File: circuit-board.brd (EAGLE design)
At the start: 40.6 x 64.1 mm, 39 parts, among them Q1 BC547B, U1 MAX3232, U2 ATMEGA328P_TQFP, U3 ADUM1201BRZ, Y1 16MHz

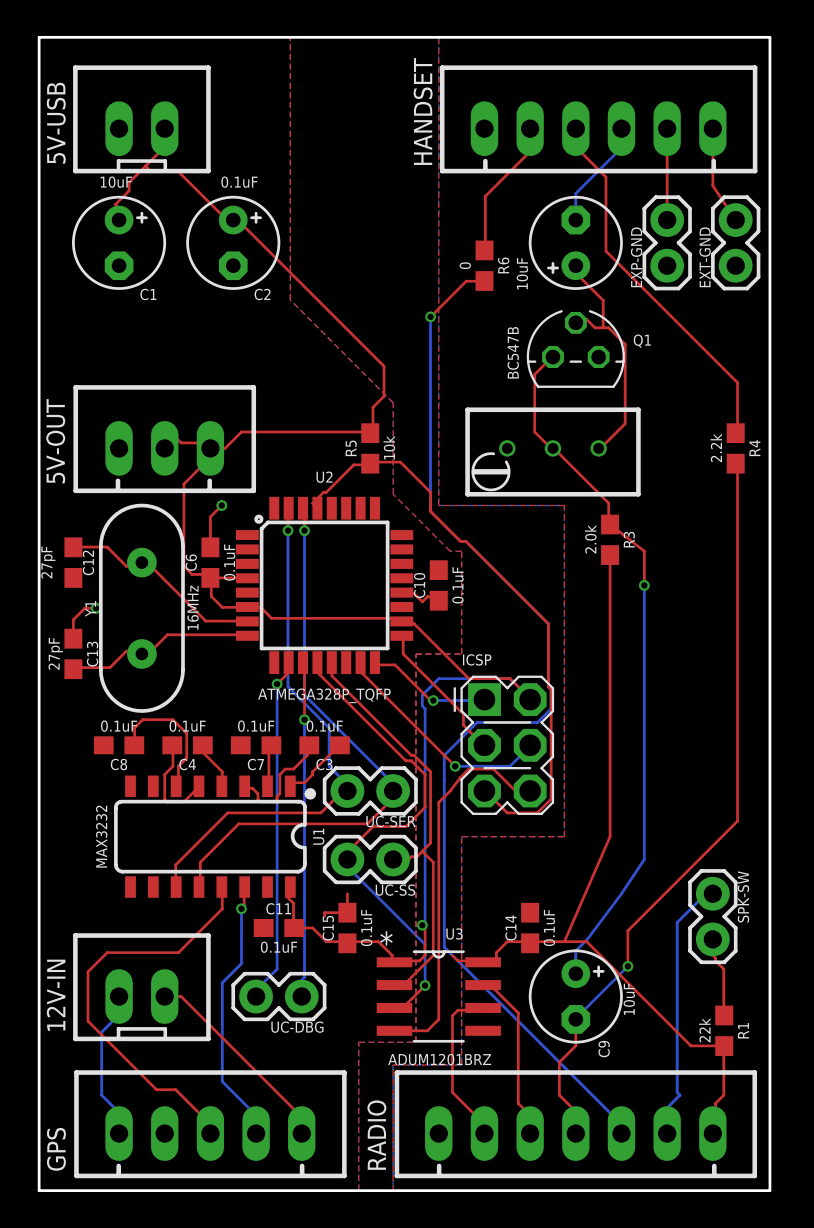
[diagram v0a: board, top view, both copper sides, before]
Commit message: Added labels for JST header pins, synced up board+schematic resistor values
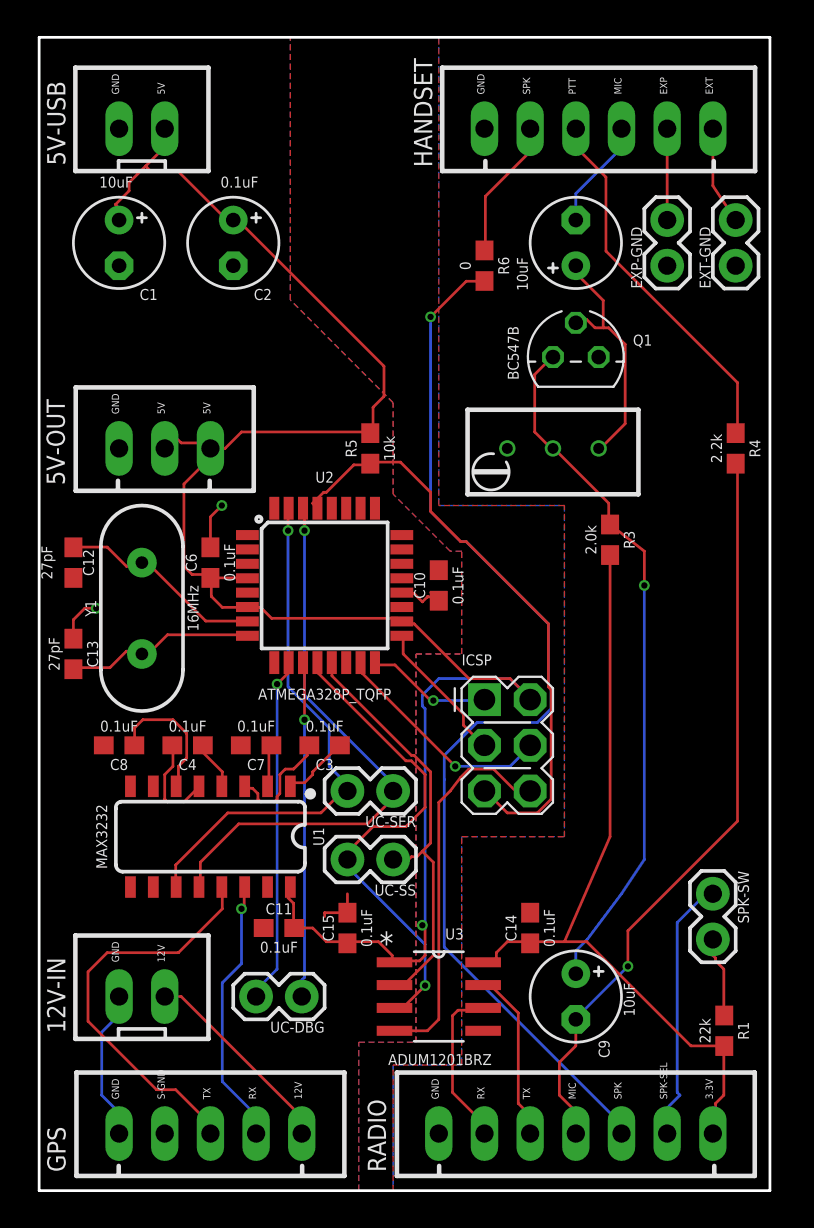
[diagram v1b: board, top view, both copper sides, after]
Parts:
- R2: value (none) -> 10k
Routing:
- net 3.3V: track 45.6 -> 43.8 mm
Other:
- board text added: "12V"
- board text added: "3.3V"
- board text added: "5V"
- board text added: "EXP"
- board text added: "EXT"
- board text added: "GND"
- board text added: "MIC"
- board text added: "PTT"
- board text added: "RX"
- board text added: "S-GND"
- board text added: "SPK"
- board text added: "SPK-SEL"
- board text added: "TX"
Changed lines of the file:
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@@
 github.com/paulmandal/radio-adapter
 v1.0</text>
+<text x="5.08" y="20.955" size="0.4064" layer="21" rot="R90">GND</text>
+<text x="7.62" y="20.955" size="0.4064" layer="21" rot="R90">S-GND</text>
+<text x="10.16" y="20.955" size="0.4064" layer="21" rot="R90">TX</text>
+<text x="12.7" y="20.955" size="0.4064" layer="21" rot="R90">RX</text>
+<text x="15.24" y="20.955" size="0.4064" layer="21" rot="R90">12V</text>
+<text x="22.86" y="20.955" size="0.4064" layer="21" rot="R90">GND</text>
+<text x="25.4" y="20.955" size="0.4064" layer="21" rot="R90">RX</text>
+<text x="27.94" y="20.955" size="0.4064" layer="21" rot="R90">TX</text>
+<text x="30.48" y="20.955" size="0.4064" layer="21" rot="R90">MIC</text>
+<text x="33.02" y="20.955" size="0.4064" layer="21" rot="R90">SPK</text>
+<text x="35.56" y="20.955" size="0.4064" layer="21" rot="R90">SPK-SEL</text>
+<text x="38.1" y="20.955" size="0.4064" layer="21" rot="R90">3.3V</text>
+<text x="5.08" y="28.575" size="0.4064" layer="21" rot="R90">GND</text>
+<text x="7.62" y="28.575" size="0.4064" layer="21" rot="R90">12V</text>
+<text x="5.08" y="59.055" size="0.4064" layer="21" rot="R90">GND</text>
+<text x="7.62" y="59.055" size="0.4064" layer="21" rot="R90">5V</text>
+<text x="10.16" y="59.055" size="0.4064" layer="21" rot="R90">5V</text>
+<text x="7.62" y="76.835" size="0.4064" layer="21" rot="R90">5V</text>
+<text x="5.08" y="76.835" size="0.4064" layer="21" rot="R90">GND</text>
+<text x="25.4" y="76.835" size="0.4064" layer="21" rot="R90">GND</text>
+<text x="27.94" y="76.835" size="0.4064" layer="21" rot="R90">SPK</text>
+<text x="30.48" y="76.835" size="0.4064" layer="21" rot="R90">PTT</text>
+<text x="33.02" y="76.835" size="0.4064" layer="21" rot="R90">MIC</text>
+<text x="35.56" y="76.835" size="0.4064" layer="21" rot="R90">EXP</text>
+<text x="38.1" y="76.835" size="0.4064" layer="21" rot="R90">EXT</text>
 </plain>
 <attributes>
@@
 <attribute name="VALUE" x="37.973" y="24.765" size="0.6096" layer="21" font="vector" ratio="20" rot="R270" align="top-center"/>
 </element>
-<element name="R2" library="resistor" library_urn="urn:adsk.eagle:library:348" package="RTRIMT93YA" package3d_urn="urn:adsk.eagle:package:26051/1" value="" x="29.21" y="57.15" smashed="yes" rot="R90">
+<element name="R2" library="resistor" library_urn="urn:adsk.eagle:library:348" package="RTRIMT93YA" package3d_urn="urn:adsk.eagle:package:26051/1" value="10k" x="29.21" y="57.15" smashed="yes" rot="R90">
 <attribute name="NAME" x="34.1" y="54.11" size="1.27" layer="27" rot="R180"/>
 <attribute name="VALUE" x="34.1" y="61.16" size="1.27" layer="27" rot="R180"/>
@@
 <wire x1="27.8892" y1="29.718" x2="27.94" y2="29.63" width="0.1524" layer="1"/>
 <wire x1="25.4508" y1="28.6512" x2="25.3238" y2="28.575" width="0.1524" layer="1"/>
-<wire x1="23.9268" y1="28.6512" x2="23.622" y2="28.956" width="0.1524" layer="1"/>
-<wire x1="25.2984" y1="28.6512" x2="23.9268" y2="28.6512" width="0.1524" layer="1"/>
 <wire x1="32.3088" y1="51.2064" x2="32.385" y2="51.22" width="0.1524" layer="1"/>
 <wire x1="25.2984" y1="28.6512" x2="25.3238" y2="28.575" width="0.1524" layer="1"/>

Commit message: Added voltage regulator, dropped some JSTs, relaid out board, rerouted
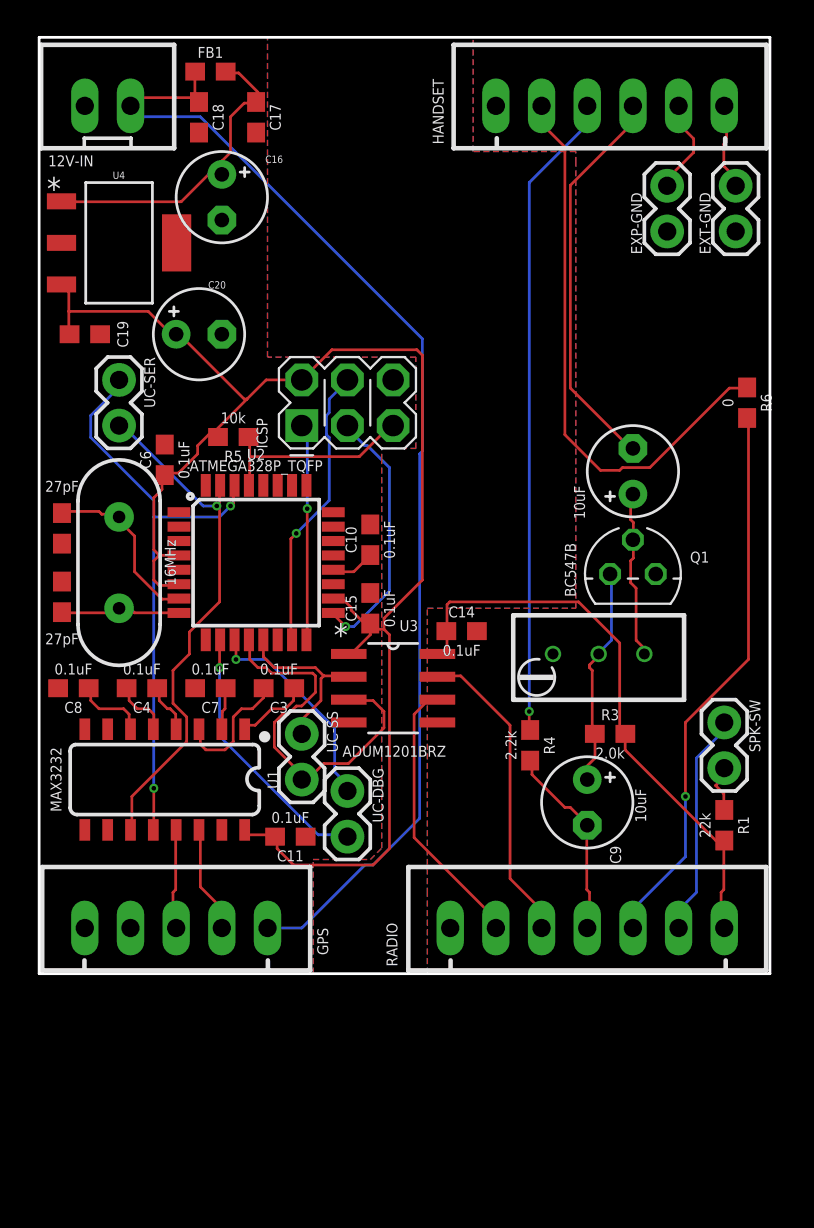
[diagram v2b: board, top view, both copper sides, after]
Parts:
- removed 5V-OUT: JST-XH-03-PIN-LONG-PAD, Rembrandt Electronics - JST XH Connectors v1-0:JST-XH-03-PACKAGE-LONG-PAD
- removed 5V-USB: JST-XH-02-PIN-LONG-PAD, Rembrandt Electronics - JST XH Connectors v1-0:JST-XH-02-PACKAGE-LONG-PAD
- removed C1: 10uF, adafruit:E2,5-5
- removed C2: 0.1uF, adafruit:E2,5-5
- added C16, C20: 10uF, adafruit:E2,5-5
- added C17, C19: 0.1uF, SparkFun-Capacitors:0603
- added C18: 10nF, SparkFun-Capacitors:0603
- added FB1: 30Ω/1.8A, SparkFun-Coils:0603
- added U4: UA78M05CDCY, Texas Instruments_By_element14_Batch_1:SOT230P700X180-4N
- moved 12V-IN 49.6 mm to (4.45, 76.2)
- moved UC-SER 27.5 mm to (5.08, 61.0), turned to 270 degrees
- moved R4 20.1 mm to (27.9, 40.6)
- moved ICSP 18.3 mm to (15.2, 58.4), turned to 90 degrees
- moved C15 17.8 mm to (19.1, 48.3)
- moved U3 17.3 mm to (20.3, 43.8)
- moved C14 16.9 mm to (24.1, 47.0), turned to 0 degrees
- moved R6 16.5 mm to (40.0, 59.7)
- moved C5 13.1 mm to (33.7, 55.9)
- moved Q1 12.5 mm to (33.7, 50.2)
- moved R2 11.7 mm to (31.8, 45.7)
- moved UC-DBG 11.7 mm to (17.8, 38.1), turned to 270 degrees
- moved GPS 11.6 mm to (8.26, 30.5)
- moved RADIO 11.4 mm to (31.1, 30.5)
- moved R1 11.4 mm to (38.7, 36.2)
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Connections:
- removed net GND2: 12V-IN.1, GPS.1
- new net N$1: C16.+, C17.1, FB1.2, U4.1
- net +5V: now also C19.1, C20.+, U4.3; no longer 5V-OUT.2, 5V-OUT.3, 5V-USB.2, C1.+, C2.+
- net 12V: now also C18.1, FB1.1
- net GNDA: now also 12V-IN.1, C16.-, C17.2, C18.2, C19.2, C20.-, GPS.1, U4.2, U4.4; no longer 5V-OUT.1, 5V-USB.1, C1.-, C2.-
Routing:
- net 12V: track 11.3 -> 65.2 mm
- net RADIO-MIC/PTT: track 41.8 -> 11.0 mm, vias 1 -> 0
- net RADIO-SPK-OUT: track 60.8 -> 31.1 mm
- net GNDA: track 28.9 -> 0.00 mm, vias 2 -> 0
- net N$3: track 38.8 -> 12.5 mm, vias 1 -> 0
- net HANDSET-SPK: track 7.80 -> 31.7 mm
- net UC-RESET: track 33.6 -> 11.5 mm
- net +5V: track 105.3 -> 86.4 mm, vias 1 -> 0
- net N$1: track 0.00 -> 17.6 mm
- net GPS-TX: track 22.6 -> 5.61 mm
- net HANDSET-MIC: track 6.13 -> 22.1 mm
- net HANDSET-PTT: track 20.7 -> 36.1 mm, vias 0 -> 1
- net UC-SS-RX: track 23.8 -> 9.89 mm
- net 3.3V: track 43.8 -> 32.4 mm
- net GPS-RX: track 15.0 -> 6.05 mm, vias 1 -> 0
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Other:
- board size 40.6 x 64.1 mm -> 40.6 x 52.1 mm
- board text removed: "5V"

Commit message: Manually routed some connections
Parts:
- moved R4 22.2 mm to (39.4, 59.7)
- moved R6 3.81 mm to (36.2, 59.7)
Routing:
- net +5V: track 86.4 -> 0.00 mm
- net UC-RX: track 32.9 -> 0.00 mm, vias 2 -> 0
- net 3.3V: track 32.4 -> 0.00 mm
- net RADIO-SPK-OUT: track 31.1 -> 0.00 mm, vias 1 -> 0
- net UC-TX: track 29.3 -> 0.00 mm, vias 1 -> 0
- net UC-SS-TX: track 21.8 -> 0.00 mm
- net N$1: track 17.6 -> 0.00 mm
- net HANDSET-PTT: track 36.1 -> 18.6 mm, vias 1 -> 0
- net RADIO-TX: track 17.2 -> 0.00 mm
- net UC-MOSI: track 16.0 -> 0.00 mm, vias 1 -> 0
- net RADIO-RX: track 15.5 -> 0.00 mm
- net UC-DBG-TX: track 14.8 -> 0.00 mm, vias 1 -> 0
- net UC-SCK: track 14.6 -> 0.00 mm, vias 1 -> 0
- net HANDSET-SPK: track 31.7 -> 18.3 mm
- net RADIO-SPK-SEL: track 12.5 -> 0.00 mm
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
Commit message: Manually routed a few more lines
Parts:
- moved R3 6.54 mm to (35.6, 35.6)
- moved C9 2.54 mm to (31.1, 40.0)
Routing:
- net 3.3V: track 0.00 -> 31.6 mm
- net N$3: track 0.00 -> 11.3 mm
- net RADIO-MIC/PTT: track 0.00 -> 8.25 mm
- net HANDSET-SPK: track 18.3 -> 18.2 mm, vias 0 -> 1
- net HANDSET-PTT: vias 0 -> 1
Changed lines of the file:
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@@
 <param name="TopRouterVariant" value="1"/>
 <param name="tpViaShape" value="round"/>
-<param name="PrefDir.1" value="a"/>
+<param name="PrefDir.1" value="|"/>
 <param name="PrefDir.2" value="0"/>
 <param name="PrefDir.3" value="0"/>
@@
 <param name="PrefDir.14" value="0"/>
 <param name="PrefDir.15" value="0"/>
-<param name="PrefDir.16" value="a"/>
+<param name="PrefDir.16" value="-"/>
 <param name="cfVia" value="8"/>
 <param name="cfNonPref" value="5"/>
@@
 <attribute name="VALUE" x="2.54" y="44.577" size="0.6096" layer="21" font="vector" ratio="20" rot="R180" align="top-center"/>
 </element>
-<element name="C9" library="adafruit" library_urn="urn:adsk.eagle:library:420" package="E2,5-5" value="10uF" x="31.115" y="37.465" smashed="yes" rot="R270">
-<attribute name="NAME" x="32.385" y="35.052" size="0.6096" layer="21" ratio="10" rot="R270"/>
-<attribute name="VALUE" x="33.782" y="38.227" size="0.6096" layer="21" ratio="10" rot="R270"/>
+<element name="C9" library="adafruit" library_urn="urn:adsk.eagle:library:420" package="E2,5-5" value="10uF" x="31.115" y="40.005" smashed="yes" rot="R270">
+<attribute name="NAME" x="32.385" y="37.592" size="0.6096" layer="21" ratio="10" rot="R270"/>
+<attribute name="VALUE" x="33.782" y="40.767" size="0.6096" layer="21" ratio="10" rot="R270"/>
 </element>
 <element name="EXP-GND" library="SparkFun-Connectors" package="1X02" value="" x="35.56" y="69.215" smashed="yes" rot="R90">
@@
 <attribute name="VALUE" x="36.63" y="46.165" size="0.6096" layer="27" rot="R270"/>
 </element>
-<element name="R3" library="SparkFun-Resistors" package="0603" value="2.0k" x="32.385" y="41.275" smashed="yes">
-<attribute name="NAME" x="32.385" y="42.037" size="0.6096" layer="25" font="vector" ratio="20" align="bottom-center"/>
-<attribute name="PROD_ID" value="RES-08296" x="32.385" y="41.275" size="1.778" layer="27" display="off"/>
-<attribute name="VALUE" x="32.385" y="40.513" size="0.6096" layer="21" font="vector" ratio="20" align="top-center"/>
+<element name="R3" library="SparkFun-Resistors" package="0603" value="2.0k" x="35.56" y="35.56" smashed="yes">
+<attribute name="NAME" x="35.56" y="36.322" size="0.6096" layer="25" font="vector" ratio="20" align="bottom-center"/>
+<attribute name="PROD_ID" value="RES-08296" x="35.56" y="35.56" size="1.778" layer="27" display="off"/>
+<attribute name="VALUE" x="35.56" y="34.798" size="0.6096" layer="21" font="vector" ratio="20" align="top-center"/>
 </element>
 <element name="R4" library="SparkFun-Resistors" package="0603" value="2.2k" x="39.37" y="59.69" smashed="yes" rot="R270">
@@
 <contactref element="U3" pad="8"/>
 <contactref element="R3" pad="2"/>
-<wire x1="38.735" y1="35.345" x2="33.235" y2="41.275" width="0" layer="19" extent="1-1"/>
-<wire x1="38.735" y1="30.48" x2="38.735" y2="35.345" width="0" layer="19" extent="1-1"/>
-<wire x1="22.7838" y1="45.72" x2="33.235" y2="41.275" width="0" layer="19" extent="1-1"/>
-<wire x1="23.28" y1="46.99" x2="22.7838" y2="45.72" width="0" layer="19" extent="1-1"/>
+<wire x1="38.735" y1="30.48" x2="38.735" y2="35.345" width="0.1524" layer="1"/>
+<wire x1="38.735" y1="35.345" x2="36.41" y2="35.56" width="0.1524" layer="1"/>
+<wire x1="36.41" y1="35.56" x2="36.195" y2="43.815" width="0.1524" layer="1"/>
+<wire x1="36.195" y1="43.815" x2="26.035" y2="43.815" width="0.1524" layer="1"/>
+<wire x1="23.28" y1="46.99" x2="22.793890625" y2="45.745828125" width="0.1524" layer="1"/>
+<wire x1="22.793890625" y1="45.745828125" x2="22.7838" y2="45.72" width="0.1524" layer="1"/>
+<wire x1="26.035" y1="43.815" x2="26.035" y2="45.085" width="0.1524" layer="1"/>
+<wire x1="26.035" y1="45.085" x2="22.793890625" y2="45.745828125" width="0.1524" layer="1"/>
 </signal>
 <signal name="GNDA">
@@
 <wire x1="28.575" y1="76.2" x2="31.115" y2="71.12" width="0.1524" layer="16"/>
 <wire x1="31.115" y1="71.12" x2="31.115" y2="66.675" width="0.1524" layer="16"/>
-<wire x1="31.115" y1="66.675" x2="36.195" y2="60.325" width="0.1524" layer="16"/>
-<wire x1="36.195" y1="60.325" x2="36.195" y2="60.54" width="0" layer="19" extent="1-16"/>
+<wire x1="31.115" y1="66.675" x2="35.56" y2="62.23" width="0.1524" layer="16"/>
+<via x="35.56" y="62.23" extent="1-16" drill="0.35"/>
+<wire x1="35.56" y1="62.23" x2="36.195" y2="60.54" width="0.1524" layer="1"/>
 </signal>
 <signal name="HANDSET-PTT">
@@
 <contactref element="R4" pad="1"/>
 <wire x1="31.115" y1="76.2" x2="33.655" y2="71.755" width="0.1524" layer="16"/>
-<wire x1="33.655" y1="71.755" x2="33.655" y2="67.31" width="0.1524" layer="16"/>
-<wire x1="33.655" y1="67.31" x2="39.37" y2="60.325" width="0.1524" layer="16"/>
-<wire x1="39.37" y1="60.325" x2="39.37" y2="60.54" width="0" layer="19" extent="1-16"/>
+<wire x1="33.655" y1="67.31" x2="33.655" y2="71.755" width="0.1524" layer="16"/>
+<wire x1="39.37" y1="60.54" x2="38.735" y2="62.23" width="0.1524" layer="1"/>
+<via x="38.735" y="62.23" extent="1-16" drill="0.35"/>
+<wire x1="38.735" y1="62.23" x2="33.655" y2="67.31" width="0.1524" layer="16"/>
 </signal>
 <signal name="HANDSET-MIC">
@@
 <contactref element="C9" pad="-"/>
 <contactref element="R4" pad="2"/>
-<wire x1="31.115" y1="36.195" x2="39.37" y2="58.84" width="0" layer="19" extent="1-1"/>
-<wire x1="31.115" y1="30.48" x2="31.115" y2="36.195" width="0" layer="19" extent="1-1"/>
+<wire x1="31.115" y1="30.48" x2="31.115" y2="38.735" width="0.1524" layer="16"/>
+<wire x1="31.115" y1="38.735" x2="39.37" y2="58.84" width="0" layer="19" extent="1-1"/>
 </signal>
 <signal name="GPS-TX">
@@
 <contactref element="R2" pad="2"/>
 <contactref element="C9" pad="+"/>
+<wire x1="34.71" y1="35.56" x2="31.115" y2="41.275" width="0.1524" layer="1"/>
+<wire x1="31.75" y1="45.72" x2="31.75" y2="42.545" width="0.1524" layer="16"/>
+<wire x1="31.75" y1="42.545" x2="31.115" y2="41.275" width="0.1524" layer="16"/>
 <wire x1="31.75" y1="45.72" x2="32.385" y2="50.165" width="0" layer="19" extent="1-1"/>
-<wire x1="31.535" y1="41.275" x2="31.75" y2="45.72" width="0" layer="19" extent="1-1"/>
-<wire x1="31.115" y1="38.735" x2="31.535" y2="41.275" width="0" layer="19" extent="1-1"/>
 </signal>
 <signal name="N$4">

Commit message: Board is final, sending to fab shop
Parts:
- removed U4: UA78M05CDCY, Texas Instruments_By_element14_Batch_1:SOT230P700X180-4N
- added IC1: UA78M05DCY, linear:SOT223
- moved UC-DBG 4.49 mm to (14.6, 41.3)
- moved UC-SS 4.07 mm to (17.8, 38.1)
- moved C14 1.27 mm to (25.4, 47.0)
- moved U3 1.27 mm to (21.6, 43.8)
- moved C16 0.63 mm to (11.4, 71.1)
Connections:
- net +5V: now also IC1.3; no longer U4.3
- net GNDA: now also IC1.2, IC1.4; no longer U4.2, U4.4
- net N$1: now also IC1.1; no longer U4.1
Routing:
- net +5V: track 0.00 -> 72.1 mm
- net UC-RX: track 0.00 -> 37.3 mm, vias 0 -> 2
- net RADIO-SPK-OUT: track 0.00 -> 29.4 mm, vias 0 -> 1
- net UC-TX: track 0.00 -> 28.6 mm, vias 0 -> 2
- net RADIO-MIC/PTT: track 8.25 -> 31.8 mm, vias 0 -> 1
- net UC-SS-TX: track 0.00 -> 18.7 mm
- net N$1: track 0.00 -> 17.0 mm
- net UC-MOSI: track 0.00 -> 16.3 mm, vias 0 -> 1
- net RADIO-TX: track 0.00 -> 16.1 mm
- net UC-SS-RX: track 0.00 -> 15.9 mm
- net RADIO-RX: track 0.00 -> 15.1 mm
- net UC-SCK: track 0.00 -> 14.0 mm, vias 0 -> 1
- net RADIO-SPK-SEL: track 0.00 -> 12.5 mm
- net UC-MISO: track 0.00 -> 12.1 mm, vias 0 -> 1
- net UC-RESET: track 0.00 -> 11.4 mm
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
